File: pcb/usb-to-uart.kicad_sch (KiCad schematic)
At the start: 16 parts, among them Q1 UMH3N, U4 CP2102N-Axx-xQFN28

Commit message: Added first version of the pcb layout
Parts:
- removed J?: Conn_01x06_Male, symbol Connector:Conn_01x06_Male
- added J13: Conn_01x04_Pin, Connector_PinHeader_2.54mm:PinHeader_1x04_P2.54mm_Vertical, symbol Connector:Conn_01x04_Pin
- J10, J11: renamed from J?; footprint (none) -> Connector_PinHeader_2.54mm:PinHeader_1x08_P2.54mm_Vertical
- gave numbers to parts that had none: 1
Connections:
- net +3V3: now also J13.1 (Pin_1)
- net EN: now also J13.4 (Pin_4)
- net GND: now also J13.2 (Pin_2)
- net IO0: now also J13.3 (Pin_3)
- no-connect marks 0 -> 4

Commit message: Try to fix all ERC and DRC Issues and Warning + changed violation config
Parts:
- removed J10, J11: Conn_01x08_Male, Connector_PinHeader_2.54mm:PinHeader_1x08_P2.54mm_Vertical, symbol Connector:Conn_01x08_Male
- added J10, J5: Conn_01x08_Pin, Connector_PinHeader_2.54mm:PinHeader_1x08_P2.54mm_Vertical, symbol Connector:Conn_01x08_Pin
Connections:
- net +3V3: now also J5.1 (Pin_1)
- net CTS: now also J10.3 (Pin_3)
- net DCD: now also J10.7 (Pin_7)
- net DSR: now also J10.5 (Pin_5)
- net DTR: now also J10.6 (Pin_6)
- net GND: now also J5.2 (Pin_2)
- net GPIO02: now also J5.3 (Pin_3)
- net GPIO03: now also J5.4 (Pin_4)
- net GPIO04: now also J10.2 (Pin_2)
- net GPIO05: now also J10.1 (Pin_1)
- net RI: now also J10.8 (Pin_8)
- net RTS: now also J10.4 (Pin_4)
- net SUSPEND: now also J5.5 (Pin_5)
- net VBUS: now also J5.8 (Pin_8)
- net ~{RST}: now also J5.7 (Pin_7)
- net ~{SUSPEND}: now also J5.6 (Pin_6)

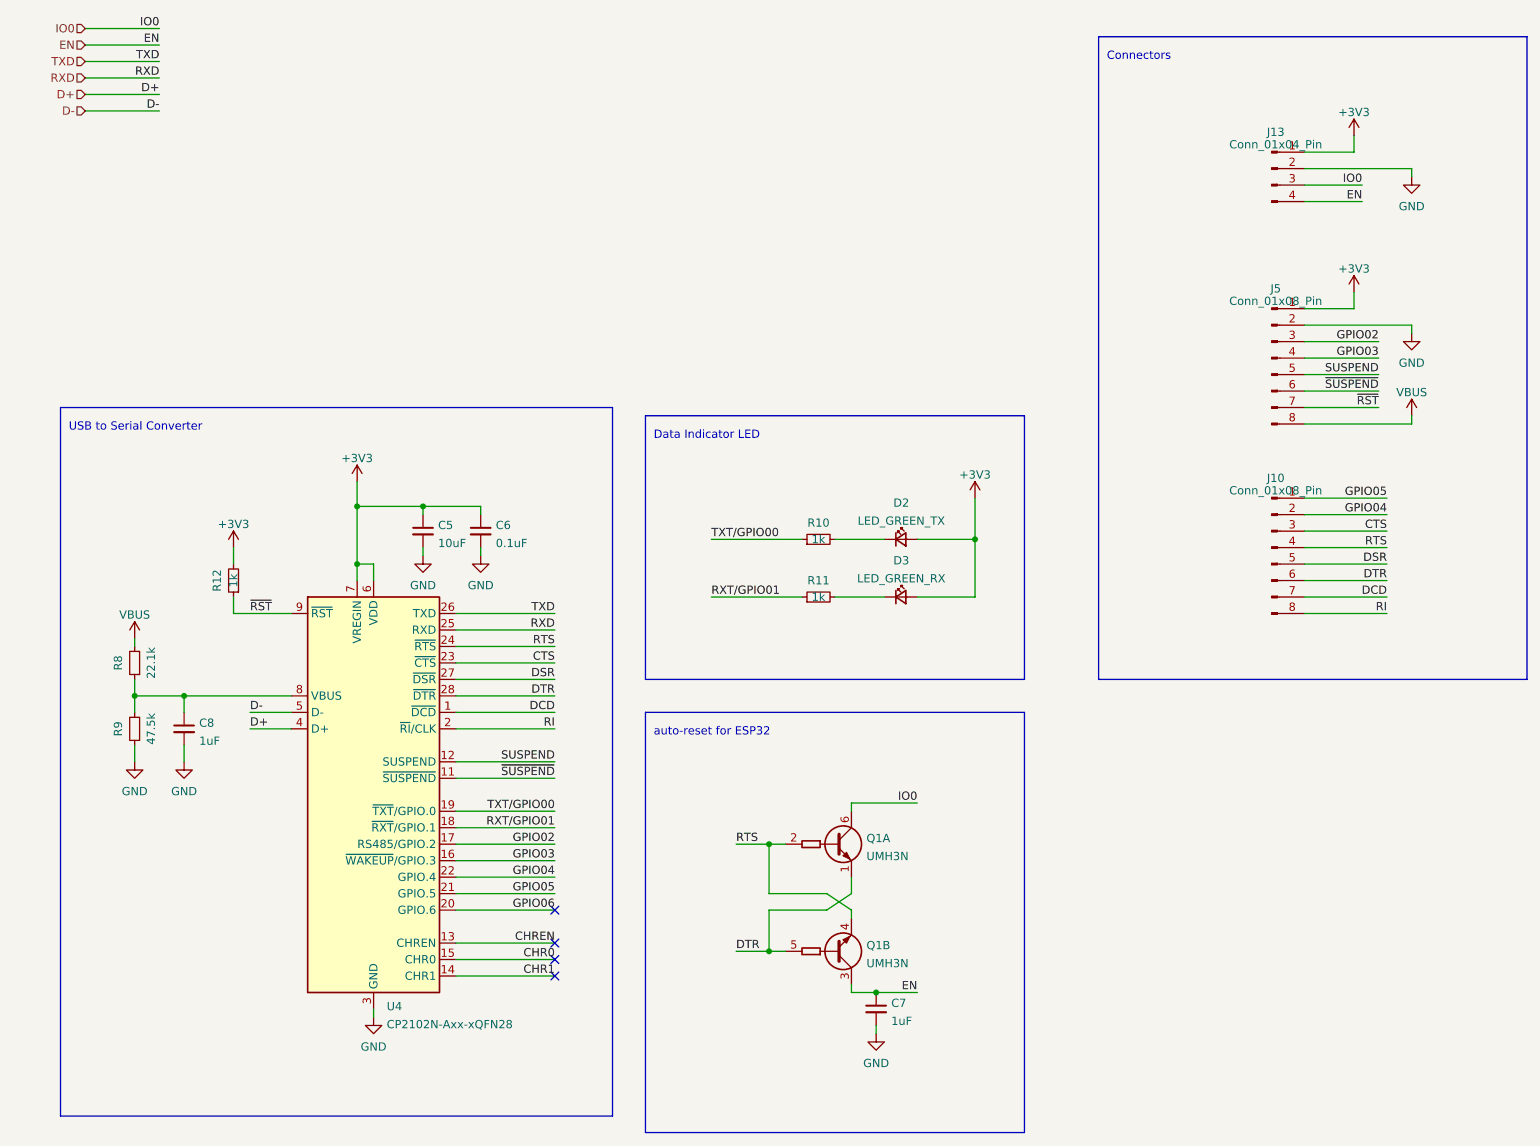
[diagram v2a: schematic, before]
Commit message: Fixed Rx Tx not being swapped between CP2102 and ESP-CM3 connector
+ Fix Label for PWR and Rx (swapped)
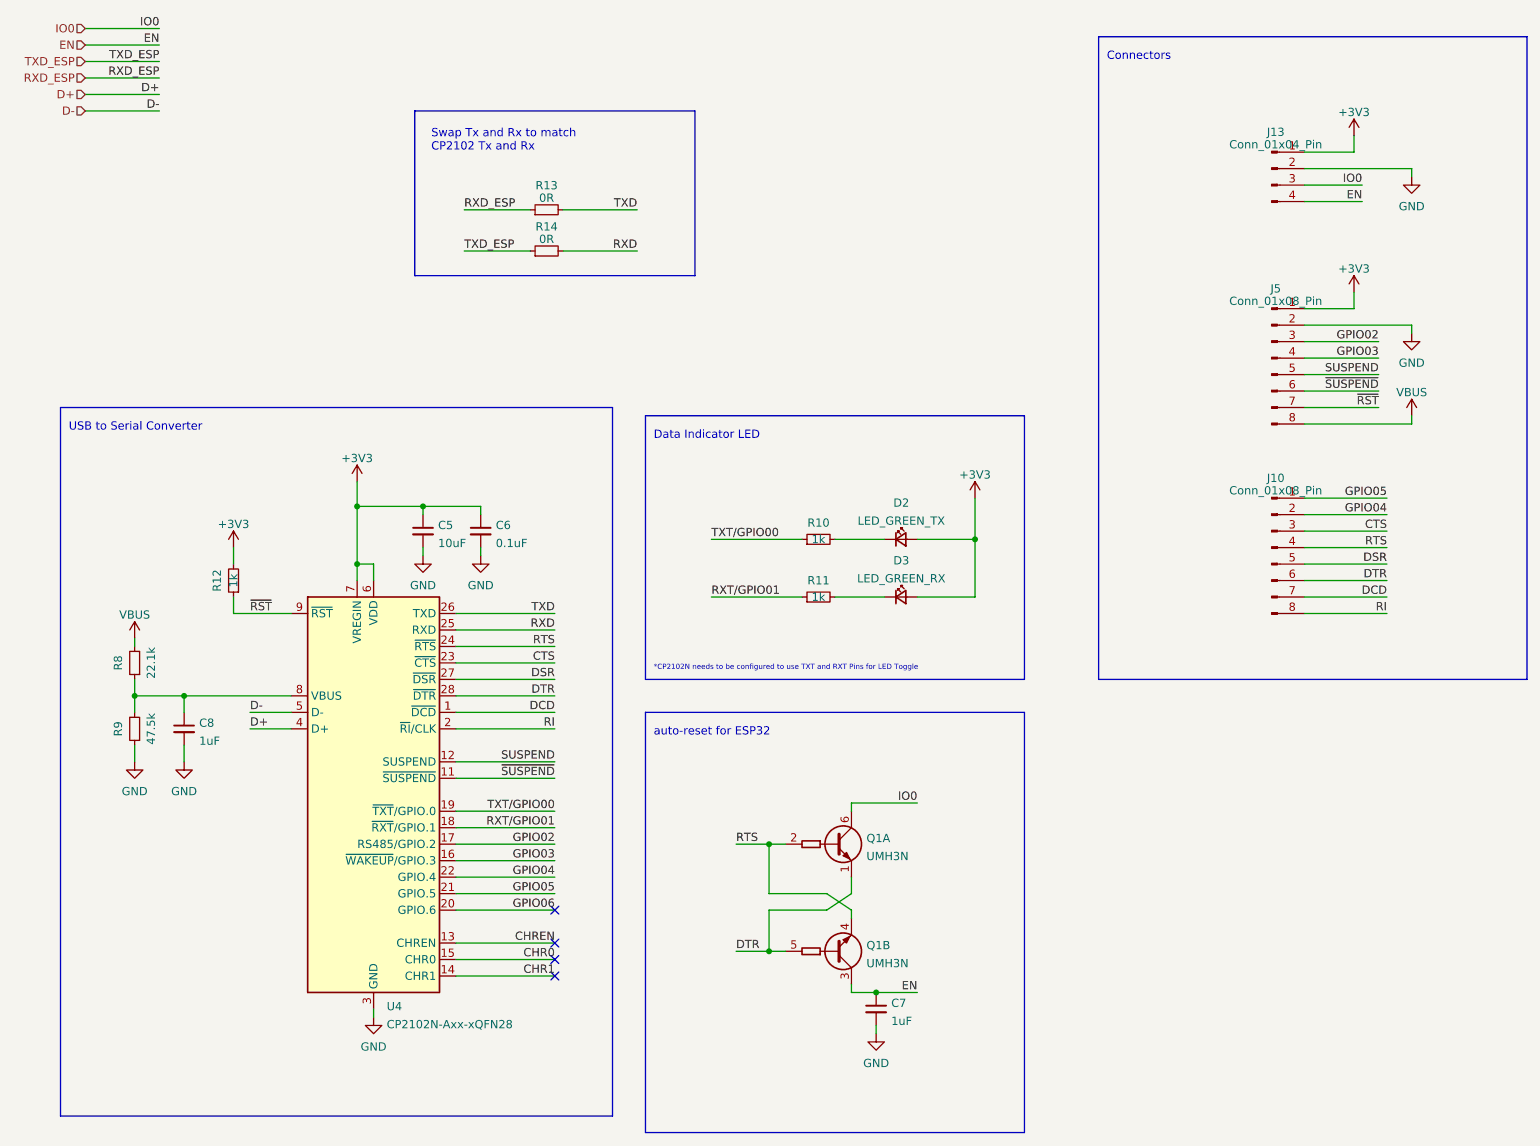
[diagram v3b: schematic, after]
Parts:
- added R13, R14: 0R, Resistor_SMD:R_0603_1608Metric, symbol Device:R_Small
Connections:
- net RXD: now also R14.2
- net TXD: now also R13.2
- new net RXD_ESP: R13.1
- new net TXD_ESP: R14.1
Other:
- note added: "*CP2102N needs to be configured to use TXT and RXT Pins for LED Toggle"
- note added: "Swap Tx and Rx to match CP2102 Tx and Rx"
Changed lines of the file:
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@@
+    (stroke (width 0) (type default))
+  )
+  (wire (pts (xy 82.55 49.53) (xy 92.71 49.53))
+    (stroke (width 0) (type default))
+  )
+  (polyline (pts (xy 74.93 34.29) (xy 118.11 34.29))
     (stroke (width 0) (type default))
   )
@@
     (stroke (width 0) (type default))
   )
+  (polyline (pts (xy 118.11 59.69) (xy 74.93 59.69))
+    (stroke (width 0) (type default))
+  )
   (wire (pts (xy 212.09 74.93) (xy 223.52 74.93))
     (stroke (width 0) (type default))
@@
     (stroke (width 0) (type default))
   )
+  (wire (pts (xy 97.79 55.88) (xy 109.22 55.88))
+    (stroke (width 0) (type default))
+  )
   (polyline (pts (xy 110.49 127) (xy 168.91 127))
     (stroke (width 0) (type default))
@@
     (stroke (width 0) (type default))
   )
+  (wire (pts (xy 82.55 55.88) (xy 92.71 55.88))
+    (stroke (width 0) (type default))
+  )
   (wire (pts (xy 81.28 162.56) (xy 96.52 162.56))
     (stroke (width 0) (type default))
   )
+  (polyline (pts (xy 74.93 59.69) (xy 74.93 34.29))
+    (stroke (width 0) (type default))
+  )
+  (polyline (pts (xy 118.11 34.29) (xy 118.11 59.69))
+    (stroke (width 0) (type default))
+  )
   (polyline (pts (xy 20.32 80.01) (xy 20.32 189.23))
     (stroke (width 0) (type default))
@@
     (stroke (width 0) (type default))
   )
+  (wire (pts (xy 97.79 49.53) (xy 109.22 49.53))
+    (stroke (width 0) (type default))
+  )
   (wire (pts (xy 139.7 100.33) (xy 147.32 100.33))
     (stroke (width 0) (type default))
@@
   (wire (pts (xy 142.24 157.48) (xy 138.43 154.94))
     (stroke (width 0) (type default))
+  )
+  (text "Swap Tx and Rx to match \nCP2102 Tx and Rx" (at 77.47 40.64 0)
+    (effects (font (size 1.27 1.27)) (justify left bottom))
   )
   (text "Connectors" (at 181.61 26.67 0)
@@
     (effects (font (size 1.27 1.27)) (justify left bottom))
   )
+  (text "*CP2102N needs to be configured to use TXT and RXT Pins for LED Toggle"
+    (at 111.76 120.65 0)
+    (effects (font (size 0.8 0.8) (color 255 249 10 1)) (justify left bottom))
+  )
   (text "Data Indicator LED " (at 111.76 85.09 0)
     (effects (font (size 1.27 1.27)) (justify left bottom))
@@
     (effects (font (size 1.27 1.27)) (justify left bottom))
   )
+  (label "RXD_ESP" (at 35.56 29.21 180) (fields_autoplaced)
+    (effects (font (size 1.27 1.27)) (justify right bottom))
+  )
   (label "SUSPEND" (at 96.52 134.62 180) (fields_autoplaced)
     (effects (font (size 1.27 1.27)) (justify right bottom))
@@
     (effects (font (size 1.27 1.27)) (justify right bottom))
   )
+  (label "RXD_ESP" (at 82.55 49.53 0) (fields_autoplaced)
+    (effects (font (size 1.27 1.27)) (justify left bottom))
+  )
   (label "IO0" (at 152.4 140.97 180) (fields_autoplaced)
     (effects (font (size 1.27 1.27)) (justify right bottom))
@@
     (effects (font (size 1.27 1.27)) (justify right bottom))
   )
-  (label "RXD" (at 35.56 29.21 180) (fields_autoplaced)
+  (label "RXD" (at 109.22 55.88 180) (fields_autoplaced)
     (effects (font (size 1.27 1.27)) (justify right bottom))
   )
@@
     (effects (font (size 1.27 1.27)) (justify right bottom))
   )
-  (label "TXD" (at 35.56 26.67 180) (fields_autoplaced)
+  (label "TXD" (at 109.22 49.53 180) (fields_autoplaced)
+    (effects (font (size 1.27 1.27)) (justify right bottom))
+  )
+  (label "TXD_ESP" (at 35.56 26.67 180) (fields_autoplaced)
     (effects (font (size 1.27 1.27)) (justify right bottom))
   )
@@
     (effects (font (size 1.27 1.27)) (justify right bottom))
   )
+  (label "TXD_ESP" (at 82.55 55.88 0) (fields_autoplaced)
+    (effects (font (size 1.27 1.27)) (justify left bottom))
+  )
   (label "EN" (at 220.98 48.26 180) (fields_autoplaced)
     (effects (font (size 1.27 1.27)) (justify right bottom))
@@
     (effects (font (size 1.27 1.27)) (justify right))
   )
-  (hierarchical_label "RXD" (shape input) (at 24.13 29.21 180) (fields_autoplaced)
+  (hierarchical_label "RXD_ESP" (shape input) (at 24.13 29.21 180) (fields_autoplaced)
     (effects (font (size 1.27 1.27)) (justify right))
   )
-  (hierarchical_label "TXD" (shape input) (at 24.13 26.67 180) (fields_autoplaced)
+  (hierarchical_label "TXD_ESP" (shape input) (at 24.13 26.67 180) (fields_autoplaced)
     (effects (font (size 1.27 1.27)) (justify right))
   )
@@
     )
   )
+  (symbol (lib_id "Device:R_Small") (at 95.25 49.53 90) (unit 1)
+    (in_bom yes) (on_board yes) (dnp no) (fields_autoplaced)
+    (property "Reference" "R13" (at 95.25 45.7835 90)
+      (effects (font (size 1.27 1.27)))
+    )
+    (property "Value" "0R" (at 95.25 47.7045 90)
+      (effects (font (size 1.27 1.27)))
+    )
+    (property "Footprint" "Resistor_SMD:R_0603_1608Metric" (at 95.25 49.53 0)
+      (effects (font (size 1.27 1.27)) hide)
+    )
+    (property "Datasheet" "~" (at 95.25 49.53 0)
+      (effects (font (size 1.27 1.27)) hide)
+    )
+    (pin "1")
+    (pin "2")
+    (instances
+      (project "so-dimm-debugger-programmer"
+        (path "/f36a67f9-a171-40fc-9f15-b33fef4bad78/5c941a60-1378-496c-a137-967d9cb608c9"
+          (reference "R13") (unit 1)
+        )
+      )
+    )
+  )
   (symbol (lib_id "Device:C_Small") (at 76.2 99.06 0) (unit 1)
     (in_bom yes) (on_board yes) (dnp no) (fields_autoplaced)
@@
         )
       )
+    )
+  )
+  (symbol (lib_id "Device:R_Small") (at 95.25 55.88 90) (unit 1)
+    (in_bom yes) (on_board yes) (dnp no) (fields_autoplaced)
+    (property "Reference" "R14" (at 95.25 52.1335 90)
+      (effects (font (size 1.27 1.27)))
+    )
+    (property "Value" "0R" (at 95.25 54.0545 90)
+      (effects (font (size 1.27 1.27)))
+    )
+    (property "Footprint" "Resistor_SMD:R_0603_1608Metric" (at 95.25 55.88 0)
+      (effects (font (size 1.27 1.27)) hide)
+    )
+    (property "Datasheet" "~" (at 95.25 55.88 0)
+      (effects (font (size 1.27 1.27)) hide)
+    )
+    (pin "1")
+    (pin "2")
+    (instances
+      (project "so-dimm-debugger-programmer"
+        (path "/f36a67f9-a171-40fc-9f15-b33fef4bad78/5c941a60-1378-496c-a137-967d9cb608c9"
+          (reference "R14") (unit 1)
+        )
+      )
